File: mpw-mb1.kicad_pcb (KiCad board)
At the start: 2 copper layers, 104.5 x 81 mm, 283 parts, among them J1 Conn_01x06, J10 Conn_01x24, J11 Conn_01x24, J2 Conn_02x02_Odd_Even, J3 613012243121, J4 Conn_01x02, J5 Conn_01x03, J6 USB_C_Receptacle_USB2.0, J7 TT03_BREAKOUT, J8 Conn_01x02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

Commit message: track cleanup, better fills
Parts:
- moved STITCH 0.10 mm to (93.9, 104.7)
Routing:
- net +3.3V: track 460.3 -> 463.4 mm
- net sel0: track 37.2 -> 36.6 mm

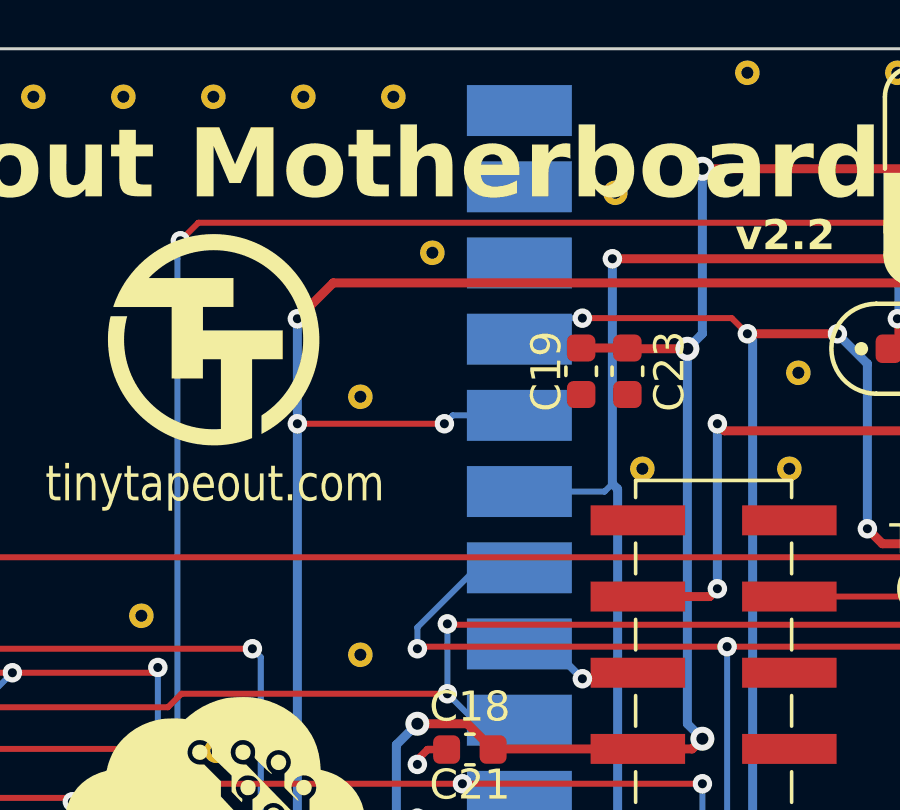
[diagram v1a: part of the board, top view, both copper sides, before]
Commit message: Move HK SPI to first CSn pin on Pico
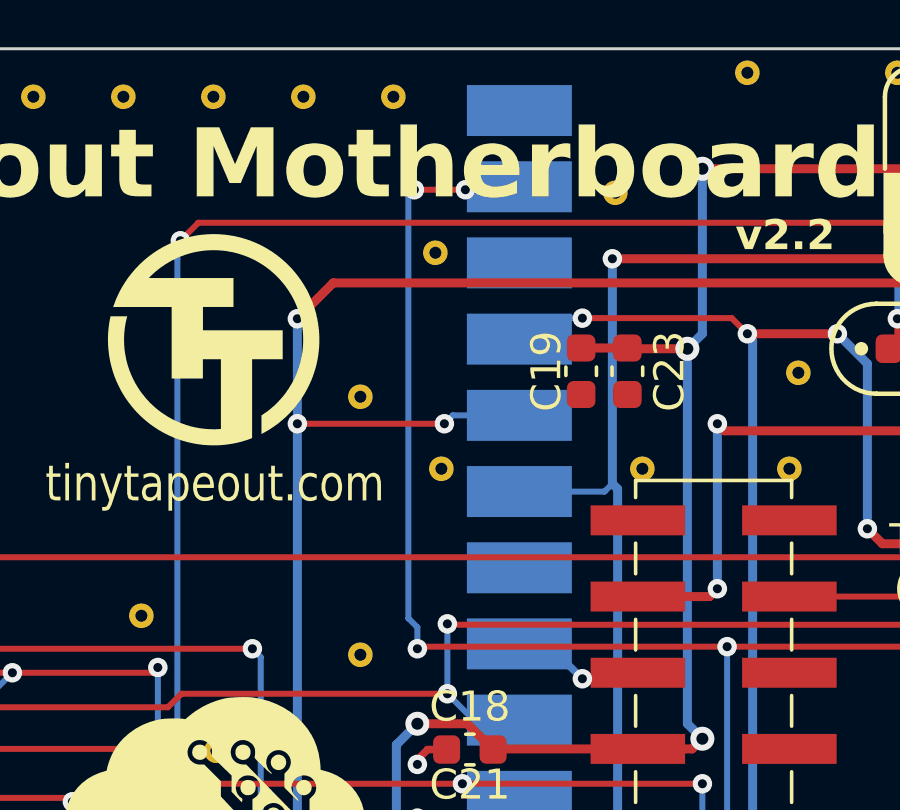
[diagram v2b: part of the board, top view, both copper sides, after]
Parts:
- added STITCH: StitchingVia-0.4mmDrill, flyingcarsfootprints:StitchingVia-0.4mmDrill, F.Cu at (114.8, 67.5)
- moved STITCH 0.10 mm to (114.6, 60.3)
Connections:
- U4 pad 2: unconnected-(U4-GPIO1-Pad2) -> mprj_io3_CSB
- U4 pad 7: mprj_io3_CSB -> unconnected-(U4-GPIO5-Pad7)
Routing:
- net mprj_io3_CSB: track 82.8 -> 96.9 mm, vias 4 -> 6
- net unconnected-(U4-GPIO5-Pad7): track 0.00 -> 0.51 mm
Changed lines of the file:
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@@
   (net 66 "Net-(J6-SHIELD)")
   (net 67 "Net-(J6-CC1)")
-  (net 68 "unconnected-(U4-GPIO1-Pad2)")
+  (net 68 "unconnected-(U4-GPIO5-Pad7)")
   (net 69 "unconnected-(J6-D+-PadA6)")
   (net 70 "unconnected-(J6-D--PadA7)")
@@
   )
   (footprint "flyingcarsfootprints:StitchingVia-0.4mmDrill" (layer "F.Cu")
+    (at 114.8 67.5)
+    (attr through_hole board_only exclude_from_pos_files exclude_from_bom)
+    (fp_text reference "STITCH" (at 0.508 1.016) (layer "F.SilkS") hide
+        (effects (font (size 1 1) (thickness 0.15)))
+    )
+    (fp_text value "StitchingVia-0.4mmDrill" (at 0 -1.016) (layer "F.Fab") hide
+        (effects (font (size 1 1) (thickness 0.15)))
+    )
+    (pad "1" thru_hole circle (at 0 0) (size 0.82 0.82) (drill 0.4) (layers "*.Cu")
+      (net 1 "GND") (zone_connect 2))
+  )
+  (footprint "flyingcarsfootprints:StitchingVia-0.4mmDrill" (layer "F.Cu")
     (at 89.2 54.3)
     (attr through_hole board_only exclude_from_pos_files exclude_from_bom)
@@
   )
   (footprint "flyingcarsfootprints:StitchingVia-0.4mmDrill" (layer "F.Cu")
-    (at 114.5 60.3)
+    (at 114.6 60.3)
     (attr through_hole board_only exclude_from_pos_files exclude_from_bom)
     (fp_text reference "STITCH" (at 0.508 1.016) (layer "F.SilkS") hide
@@
       (stroke (width 0.12) (type solid)) (layer "B.Fab"))
     (pad "1" smd rect locked (at -8.89 24.13 180) (size 3.5 1.7) (drill (offset -0.9 0)) (layers "B.Cu" "B.Mask")
-      (net 106 "unconnected-(U4-GPIO0-Pad1)") (pinfunction "GPIO0") (pintype "bidirectional"))
+      (net 106 "unconnected-(U4-GPIO0-Pad1)") (pinfunction "GPIO0") (pintype "bidirectional+no_connect"))
     (pad "2" smd rect locked (at -8.89 21.59 180) (size 3.5 1.7) (drill (offset -0.9 0)) (layers "B.Cu" "B.Mask")
-      (net 68 "unconnected-(U4-GPIO1-Pad2)") (pinfunction "GPIO1") (pintype "bidirectional"))
+      (net 23 "mprj_io3_CSB") (pinfunction "GPIO1") (pintype "bidirectional"))
     (pad "3" smd rect locked (at -8.89 19.05 180) (size 3.5 1.7) (drill (offset -0.9 0)) (layers "B.Cu" "B.Mask")
       (net 1 "GND") (pinfunction "GND") (pintype "power_in"))
@@
       (net 25 "mprj_io1_SDO") (pinfunction "GPIO4") (pintype "bidirectional"))
     (pad "7" smd rect locked (at -8.89 8.89 180) (size 3.5 1.7) (drill (offset -0.9 0)) (layers "B.Cu" "B.Mask")
-      (net 23 "mprj_io3_CSB") (pinfunction "GPIO5") (pintype "bidirectional"))
+      (net 68 "unconnected-(U4-GPIO5-Pad7)") (pinfunction "GPIO5") (pintype "bidirectional+no_connect"))
     (pad "8" smd rect locked (at -8.89 6.35 180) (size 3.5 1.7) (drill (offset -0.9 0)) (layers "B.Cu" "B.Mask")
       (net 1 "GND") (pinfunction "GND") (pintype "power_in"))
@@
       (net 1 "GND") (pinfunction "GND") (pintype "power_in"))
     (pad "14" smd rect locked (at -8.89 -8.89 180) (size 3.5 1.7) (drill (offset -0.9 0)) (layers "B.Cu" "B.Mask")
-      (net 96 "unconnected-(U4-GPIO10-Pad14)") (pinfunction "GPIO10") (pintype "bidirectional"))
+      (net 96 "unconnected-(U4-GPIO10-Pad14)") (pinfunction "GPIO10") (pintype "bidirectional+no_connect"))
     (pad "15" smd rect locked (at -8.89 -11.43 180) (size 3.5 1.7) (drill (offset -0.9 0)) (layers "B.Cu" "B.Mask")
-      (net 97 "unconnected-(U4-GPIO11-Pad15)") (pinfunction "GPIO11") (pintype "bidirectional"))
+      (net 97 "unconnected-(U4-GPIO11-Pad15)") (pinfunction "GPIO11") (pintype "bidirectional+no_connect"))
     (pad "16" smd rect locked (at -8.89 -13.97 180) (size 3.5 1.7) (drill (offset -0.9 0)) (layers "B.Cu" "B.Mask")
-      (net 98 "unconnected-(U4-GPIO12-Pad16)") (pinfunction "GPIO12") (pintype "bidirectional"))
+      (net 98 "unconnected-(U4-GPIO12-Pad16)") (pinfunction "GPIO12") (pintype "bidirectional+no_connect"))
     (pad "17" smd rect locked (at -8.89 -16.51 180) (size 3.5 1.7) (drill (offset -0.9 0)) (layers "B.Cu" "B.Mask")
-      (net 99 "unconnected-(U4-GPIO13-Pad17)") (pinfunction "GPIO13") (pintype "bidirectional"))
+      (net 99 "unconnected-(U4-GPIO13-Pad17)") (pinfunction "GPIO13") (pintype "bidirectional+no_connect"))
     (pad "18" smd rect locked (at -8.89 -19.05 180) (size 3.5 1.7) (drill (offset -0.9 0)) (layers "B.Cu" "B.Mask")
       (net 1 "GND") (pinfunction "GND") (pintype "power_in"))
@@
   (segment (start 124.325 73.430676) (end 114.069324 73.430676) (width 0.2) (layer "F.Cu") (net 23))
   (segment (start 126.2 99.5) (end 126.4 99.7) (width 0.2) (layer "F.Cu") (net 23))
+  (segment (start 113.9 58.2) (end 115.599998 58.2) (width 0.2) (layer "F.Cu") (net 23))
   (segment (start 153.5 72.5) (end 133.4 72.5) (width 0.2) (layer "F.Cu") (net 23))
   (segment (start 124.5 99.5) (end 126.2 99.5) (width 0.2) (layer "F.Cu") (net 23))
@@
   (segment (start 133.4 72.5) (end 132.469324 73.430676) (width 0.2) (layer "F.Cu") (net 23))
   (segment (start 132.469324 73.430676) (end 124.325 73.430676) (width 0.2) (layer "F.Cu") (net 23))
+  (via (at 113.9 58.2) (size 0.65) (drill 0.3) (layers "F.Cu" "B.Cu") (net 23))
   (via (at 124.5 99.5) (size 0.65) (drill 0.3) (layers "F.Cu" "B.Cu") (net 23))
   (via (at 124.325 73.430676) (size 0.65) (drill 0.3) (layers "F.Cu" "B.Cu") (net 23))
   (via (at 153.5 72.5) (size 0.65) (drill 0.3) (layers "F.Cu" "B.Cu") (net 23))
   (via (at 114 73.5) (size 0.65) (drill 0.3) (layers "F.Cu" "B.Cu") (net 23))
+  (via (at 115.599998 58.2) (size 0.65) (drill 0.3) (layers "F.Cu" "B.Cu") (net 23))
+  (segment (start 114 72.786116) (end 113.7 72.486116) (width 0.2) (layer "B.Cu") (net 23))
+  (segment (start 116.4 58.2) (end 116.5 58.1) (width 0.2) (layer "B.Cu") (net 23))
   (segment (start 124.325 73.430676) (end 124.325 99.325) (width 0.2) (layer "B.Cu") (net 23))
+  (segment (start 114 73.5) (end 114 72.786116) (width 0.2) (layer "B.Cu") (net 23))
   (segment (start 153.5 77.18) (end 153.5 72.5) (width 0.2) (layer "B.Cu") (net 23))
-  (segment (start 114 72.786116) (end 115.986116 70.8) (width 0.2) (layer "B.Cu") (net 23))
-  (segment (start 115.986116 70.8) (end 116.5 70.8) (width 0.2) (layer "B.Cu") (net 23))
+  (segment (start 115.599998 58.2) (end 116.4 58.2) (width 0.2) (layer "B.Cu") (net 23))
+  (segment (start 113.7 58.4) (end 113.9 58.2) (width 0.2) (layer "B.Cu") (net 23))
   (segment (start 124.325 99.325) (end 124.5 99.5) (width 0.2) (layer "B.Cu") (net 23))
-  (segment (start 114 73.5) (end 114 72.786116) (width 0.2) (layer "B.Cu") (net 23))
   (segment (start 157.8 81.48) (end 153.5 77.18) (width 0.2) (layer "B.Cu") (net 23))
+  (segment (start 113.7 72.486116) (end 113.7 58.4) (width 0.2) (layer "B.Cu") (net 23))
   (segment (start 110.000008 62.499992) (end 110.000008 62.5) (width 0.3) (layer "F.Cu") (net 24))
   (segment (start 154.5 62) (end 153.805 61.305) (width 0.3) (layer "F.Cu") (net 24))
@@
   (segment (start 65.6 126.4) (end 65.68 126.48) (width 0.2) (layer "B.Cu") (net 66))
   (segment (start 68.75 124.075) (end 68.75 127.955) (width 0.2) (layer "F.Cu") (net 67))
+  (segment (start 115.986116 70.8) (end 116.5 70.8) (width 0.2) (layer "B.Cu") (net 68))
   (segment (start 71.75 127.955) (end 71.75 126.75) (width 0.2) (layer "F.Cu") (net 71))
   (segment (start 71.75 126.75) (end 70.57 125.57) (width 0.2) (layer "F.Cu") (net 71))

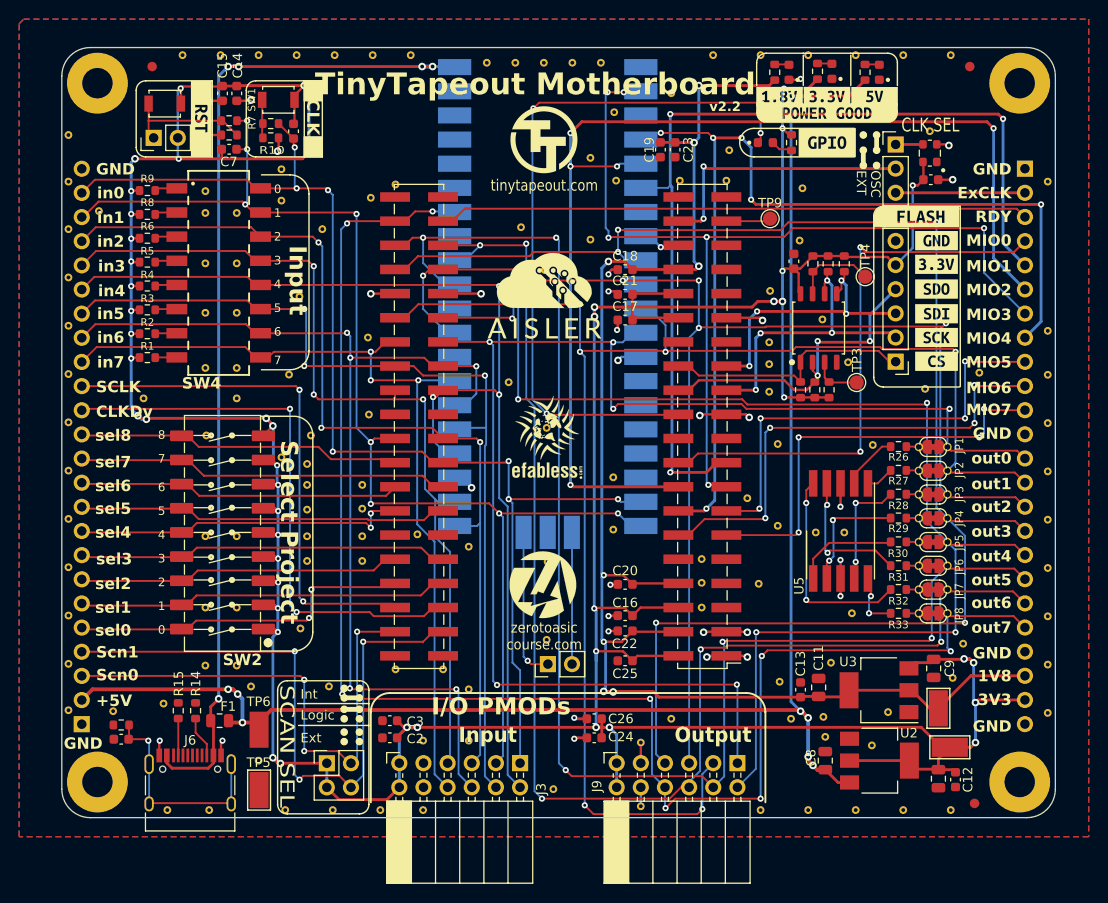
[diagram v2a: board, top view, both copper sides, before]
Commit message: v2.2.2: part swaps as per Aisler requests, re-route relevant sections
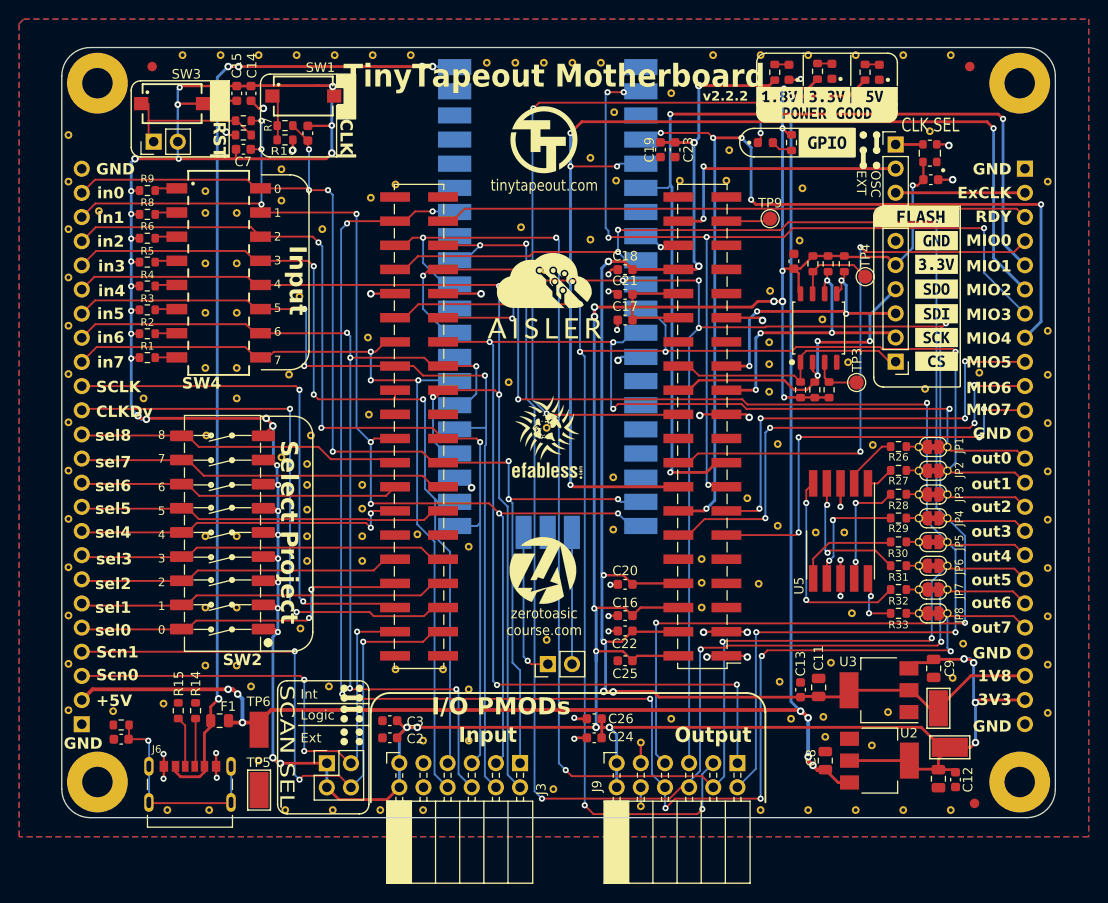
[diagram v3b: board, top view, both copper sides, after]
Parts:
- removed kibuzzard-63FE3D95: G***, kibuzzard-63FE3D95
- J6: value USB_C_Receptacle_USB2.0 -> UJC-HP-3-SMT-TR; footprint Connector_USB:USB_C_Receptacle_HRO_TYPE-C-31-M-12 -> TinyTapeout:CUI_UJC-HP-3-SMT-TR
- SW1, SW3: footprint Button_Switch_SMD:SW_SPST_B3U-1000P -> TinyTapeout:434121025816
- moved J6 2.90 mm to (70.0, 129.1)
- moved SW1 2.66 mm to (81.9, 58.6)
- moved C1 1.51 mm to (82.4, 62.5)
- moved R10 1.51 mm to (80.0, 63.2)
- moved R7 1.51 mm to (80.0, 61.7)
- moved C14 1.50 mm to (76.4, 58.3)
- moved C15 1.50 mm to (74.9, 58.3)
- moved C7 1.50 mm to (75.6, 64.2)
- moved R20 1.50 mm to (75.6, 61.2)
- moved R21 1.50 mm to (75.6, 62.7)
- moved REF** 1.50 mm to (107.2, 108.4)
- moved SW3 0.77 mm to (68.1, 59.4)
- moved J4 0.40 mm to (66.2, 63.4)
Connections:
- C4 pad 1: Net-(J6-SHIELD) -> Net-(C4-Pad1)
- J6 pad S1: Net-(J6-SHIELD) -> Net-(C4-Pad1)
- R11 pad 1: Net-(J6-SHIELD) -> Net-(C4-Pad1)
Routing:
- net Net-(J6-SHIELD): track 23.2 -> 0.00 mm, vias 1 -> 0
- net Net-(C4-Pad1): track 0.00 -> 23.2 mm, vias 0 -> 1
- net +3.3V: track 463.4 -> 467.4 mm, vias 46 -> 48
- net Net-(J4-Pin_1): track 13.7 -> 15.6 mm
- net VBUS: track 107.2 -> 105.8 mm
- net Net-(J6-CC1): track 3.88 -> 5.32 mm
- net GND: track 66.0 -> 67.2 mm, vias 32 -> 34
- net Net-(J6-CC2): track 4.37 -> 5.06 mm
- net Net-(R10-Pad1): track 4.03 -> 4.68 mm
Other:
- board text added: "MIO1/SDO"
- board text added: "MIO2/SDI"
- board text added: "MIO3/CSB"
- board text added: "MIO4/SCK"
- board text added: "MIO5/RX"
- board text added: "MIO6/TX"
- board text added: "RST"
- board text added: "v2.2.2"
- board text removed: "v2.2"
